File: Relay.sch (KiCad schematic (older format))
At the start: 0 parts

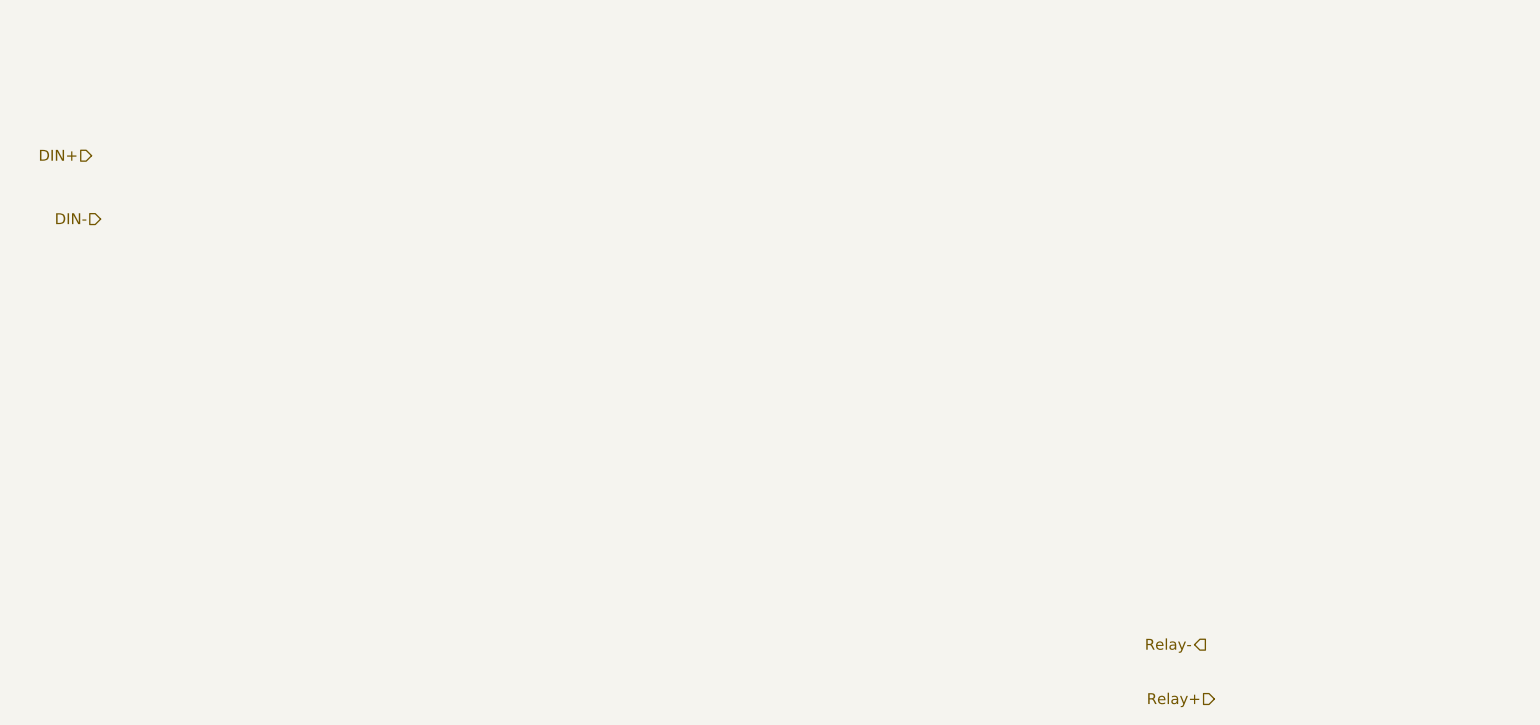
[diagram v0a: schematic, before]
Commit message: Added Powercontrol stuff
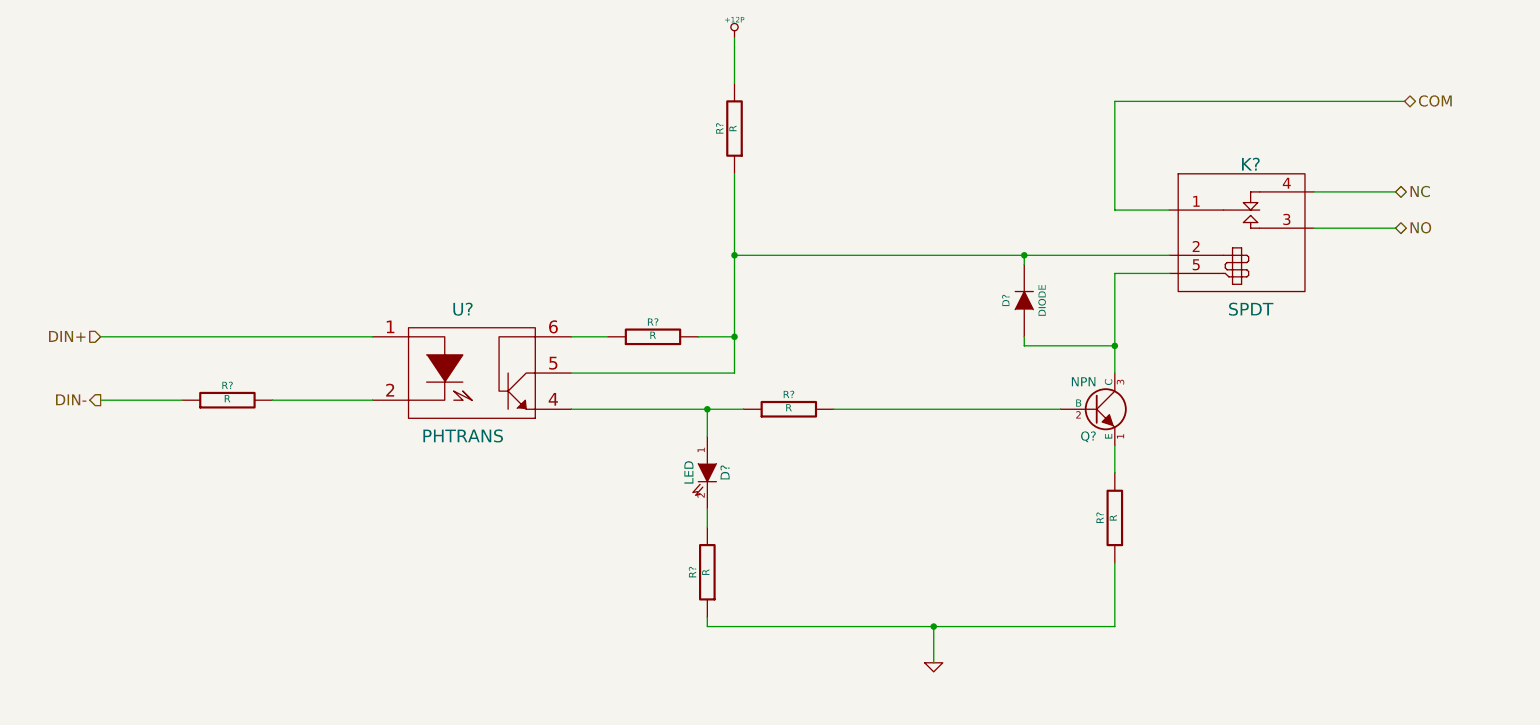
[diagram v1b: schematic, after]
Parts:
- added D?: LED, ~, symbol LED
- added D?: DIODE, ~, symbol DIODE
- added K?: SPDT, ~, symbol SPDT
- added Q?: NPN, ~, symbol NPN
- added R? (x6): R, ~, symbol R
- added U?: PHTRANS, ~, symbol PHTRANS
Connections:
- net DIN+: now also U?.1
- net DIN-: now also R?.1
- new net: R?.2, U?.2
- new net: D?.1 (A), R?.1, U?.4
- new net: D?.2 (K), K?.2 (COIL+), R?.1, R?.2, U?.5
- new net: R?.1, U?.6
- new net: Q?.2 (B), R?.2
- new net: Q?.1 (E), R?.2
- new net: D?.1 (A), K?.5 (COIL-), Q?.3 (C)
- new net: D?.2 (K), R?.2
- new net +12P: R?.2
- new net COM: K?.1 (COM)
- new net GND: R?.1, R?.1
- new net NC: K?.4 (NC)
- new net NO: K?.3 (NO)
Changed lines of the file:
@@
 LIBS:contrib
 LIBS:valves
+LIBS:BenchBuddy
 LIBS:BenchBuddy-cache
 EELAYER 27 0
@@
 $Descr A4 11693 8268
 encoding utf-8
-Sheet 4 8
+Sheet 4 9
 Title ""
-Date "31 jan 2014"
+Date "4 feb 2014"
 Rev ""
 Comp ""
@@
 Comment4 ""
 $EndDescr
-Text HLabel 2800 1950 0    60   Input ~ 0
+Text HLabel 2850 2950 0    60   Input ~ 0
 DIN+
-Text HLabel 2850 2300 0    60   Input ~ 0
+Text HLabel 2850 3300 0    60   Output ~ 0
 DIN-
-Text HLabel 8950 4650 0    60   Output ~ 0
-Relay-
-Text HLabel 9000 4950 0    60   Input ~ 0
-Relay+
+Text HLabel 10000 2350 2    60   BiDi ~ 0
+NO
+Text HLabel 10000 2150 2    60   BiDi ~ 0
+NC
+$Comp
+L PHTRANS U?
+U 1 1 52F0ACE1
+P 4900 3150
+F 0 "U?" H 4850 3500 70  0000 C CNN
+F 1 "PHTRANS" H 4850 2800 70  0000 C CNN
+F 2 "~" H 4900 3150 60  0000 C CNN
+F 3 "~" H 4900 3150 60  0000 C CNN
+	1    4900 3150
+	1    0    0    -1
+$EndComp
+$Comp
+L R R?
+U 1 1 52F0AD0D
+P 6650 3350
+F 0 "R?" V 6730 3350 40  0000 C CNN
+F 1 "R" V 6657 3351 40  0000 C CNN
+F 2 "~" V 6580 3350 30  0000 C CNN
+F 3 "~" H 6650 3350 30  0000 C CNN
+	1    6650 3350
+	0    -1   -1   0
+$EndComp
+$Comp
+L NPN Q?
+U 1 1 52F0AD1C
+P 8350 3350
+F 0 "Q?" H 8350 3200 50  0000 R CNN
+F 1 "NPN" H 8350 3500 50  0000 R CNN
+F 2 "~" H 8350 3350 60  0000 C CNN
+F 3 "~" H 8350 3350 60  0000 C CNN
+	1    8350 3350
+	1    0    0    -1
+$EndComp
+$Comp
+L LED D?
+U 1 1 52F0AD2B
+P 6200 3700
+F 0 "D?" H 6200 3800 50  0000 C CNN
+F 1 "LED" H 6200 3600 50  0000 C CNN
+F 2 "~" H 6200 3700 60  0000 C CNN
+F 3 "~" H 6200 3700 60  0000 C CNN
+	1    6200 3700
+	0    1    1    0
+$EndComp
+$Comp
+L SPDT K?
+U 1 1 52F0B440
+P 9200 2450
+F 0 "K?" H 9200 2900 70  0000 C CNN
+F 1 "SPDT" H 9200 2100 70  0000 C CNN
+F 2 "~" H 9150 2700 60  0000 C CNN
+F 3 "~" H 9150 2700 60  0000 C CNN
+	1    9200 2450
+	1    0    0    -1
+$EndComp
+Text HLabel 10050 1650 2    60   BiDi ~ 0
+COM
+Wire Wire Line
+	10000 2150 9550 2150
+Wire Wire Line
+	10000 2350 9550 2350
+Wire Wire Line
+	5450 3350 6400 3350
+$Comp
+L R R?
+U 1 1 52F0B4B2
+P 8450 3950
+F 0 "R?" V 8530 3950 40  0000 C CNN
+F 1 "R" V 8457 3951 40  0000 C CNN
+F 2 "~" V 8380 3950 30  0000 C CNN
+F 3 "~" H 8450 3950 30  0000 C CNN
+	1    8450 3950
+	-1   0    0    1
+$EndComp
+$Comp
+L GND #PWR?
+U 1 1 52F0B4BA
+P 7450 4750
+F 0 "#PWR?" H 7450 4750 30  0001 C CNN
+F 1 "GND" H 7450 4680 30  0001 C CNN
+F 2 "" H 7450 4750 60  0000 C CNN
+F 3 "" H 7450 4750 60  0000 C CNN
+	1    7450 4750
+	1    0    0    -1
+$EndComp
+Wire Wire Line
+	8450 3550 8450 3700
+$Comp
+L R R?
+U 1 1 52F0B4EC
+P 6350 1800
+F 0 "R?" V 6430 1800 40  0000 C CNN
+F 1 "R" V 6357 1801 40  0000 C CNN
+F 2 "~" V 6280 1800 30  0000 C CNN
+F 3 "~" H 6350 1800 30  0000 C CNN
+	1    6350 1800
+	-1   0    0    1
+$EndComp
+$Comp
+L R R?
+U 1 1 52F0B501
+P 6200 4250
+F 0 "R?" V 6280 4250 40  0000 C CNN
+F 1 "R" V 6207 4251 40  0000 C CNN
+F 2 "~" V 6130 4250 30  0000 C CNN
+F 3 "~" H 6200 4250 30  0000 C CNN
+	1    6200 4250
+	-1   0    0    1
+$EndComp
+Wire Wire Line
+	6200 3350 6200 3500
+Wire Wire Line
+	6200 3900 6200 4000
+Wire Wire Line
+	6200 4500 6200 4550
+Wire Wire Line
+	6200 4550 8450 4550
+Connection ~ 7450 4550
+Wire Wire Line
+	6350 2050 6350 3150
+Connection ~ 6350 2500
+$Comp
+L R R?
+U 1 1 52F0B56E
+P 5900 2950
+F 0 "R?" V 5980 2950 40  0000 C CNN
+F 1 "R" V 5907 2951 40  0000 C CNN
+F 2 "~" V 5830 2950 30  0000 C CNN
+F 3 "~" H 5900 2950 30  0000 C CNN
+	1    5900 2950
+	0    -1   -1   0
+$EndComp
+Wire Wire Line
+	6350 3150 5450 3150
+Connection ~ 6200 3350
+Wire Wire Line
+	6150 2950 6350 2950
+Connection ~ 6350 2950
+Wire Wire Line
+	5650 2950 5450 2950
+Wire Wire Line
+	6350 1300 6350 1550
+$Comp
+L R R?
+U 1 1 52F0B602
+P 3550 3300
+F 0 "R?" V 3630 3300 40  0000 C CNN
+F 1 "R" V 3557 3301 40  0000 C CNN
+F 2 "~" V 3480 3300 30  0000 C CNN
+F 3 "~" H 3550 3300 30  0000 C CNN
+	1    3550 3300
+	0    -1   -1   0
+$EndComp
+Wire Wire Line
+	2850 2950 4350 2950
+Wire Wire Line
+	2850 3300 3300 3300
+Wire Wire Line
+	3800 3300 4350 3300
+Wire Wire Line
+	8750 2500 6350 2500
+Wire Wire Line
+	8450 2600 8450 3150
+Wire Wire Line
+	8750 2250 8450 2250
+Wire Wire Line
+	8450 2250 8450 1650
+Wire Wire Line
+	8450 1650 10050 1650
+Wire Wire Line
+	8150 3350 6900 3350
+Wire Wire Line
+	7450 4550 7450 4750
+Wire Wire Line
+	8450 4550 8450 4200
+Wire Wire Line
+	8750 2600 8450 2600
+$Comp
+L DIODE D?
+U 1 1 52F0B784
+P 7950 2750
+F 0 "D?" H 7950 2850 40  0000 C CNN
+F 1 "DIODE" H 7950 2650 40  0000 C CNN
+F 2 "~" H 7950 2750 60  0000 C CNN
+F 3 "~" H 7950 2750 60  0000 C CNN
+	1    7950 2750
+	0    -1   -1   0
+$EndComp
+Wire Wire Line
+	7950 2550 7950 2500
+Connection ~ 7950 2500
+Wire Wire Line
+	7950 2950 7950 3000
+Wire Wire Line
+	7950 3000 8450 3000
+Connection ~ 8450 3000
+$Comp
+L +12P #PWR?
+U 1 1 52F1085D
+P 6350 1300
+F 0 "#PWR?" H 6350 1270 30  0001 C CNN
+F 1 "+12P" H 6350 1400 30  0000 C CNN
+F 2 "" H 6350 1300 60  0000 C CNN
+F 3 "" H 6350 1300 60  0000 C CNN
+	1    6350 1300
+	1    0    0    -1
+$EndComp
 $EndSCHEMATC

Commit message: Struktur nach Arduino
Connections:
- net COM renamed RELAY_COM
- net DIN+ renamed RELAY+
- net DIN- renamed RELAY-
- net NC renamed RELAY_NC
- net NO renamed RELAY_NO
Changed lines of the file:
@@
 Sheet 4 9
 Title ""
-Date "4 feb 2014"
+Date "6 feb 2014"
 Rev ""
 Comp ""
@@
 $EndDescr
 Text HLabel 2850 2950 0    60   Input ~ 0
-DIN+
+RELAY+
 Text HLabel 2850 3300 0    60   Output ~ 0
-DIN-
+RELAY-
 Text HLabel 10000 2350 2    60   BiDi ~ 0
-NO
+RELAY_NO
 Text HLabel 10000 2150 2    60   BiDi ~ 0
-NC
+RELAY_NC
 $Comp
 L PHTRANS U?
@@
 $EndComp
 Text HLabel 10050 1650 2    60   BiDi ~ 0
-COM
+RELAY_COM
 Wire Wire Line
 	10000 2150 9550 2150

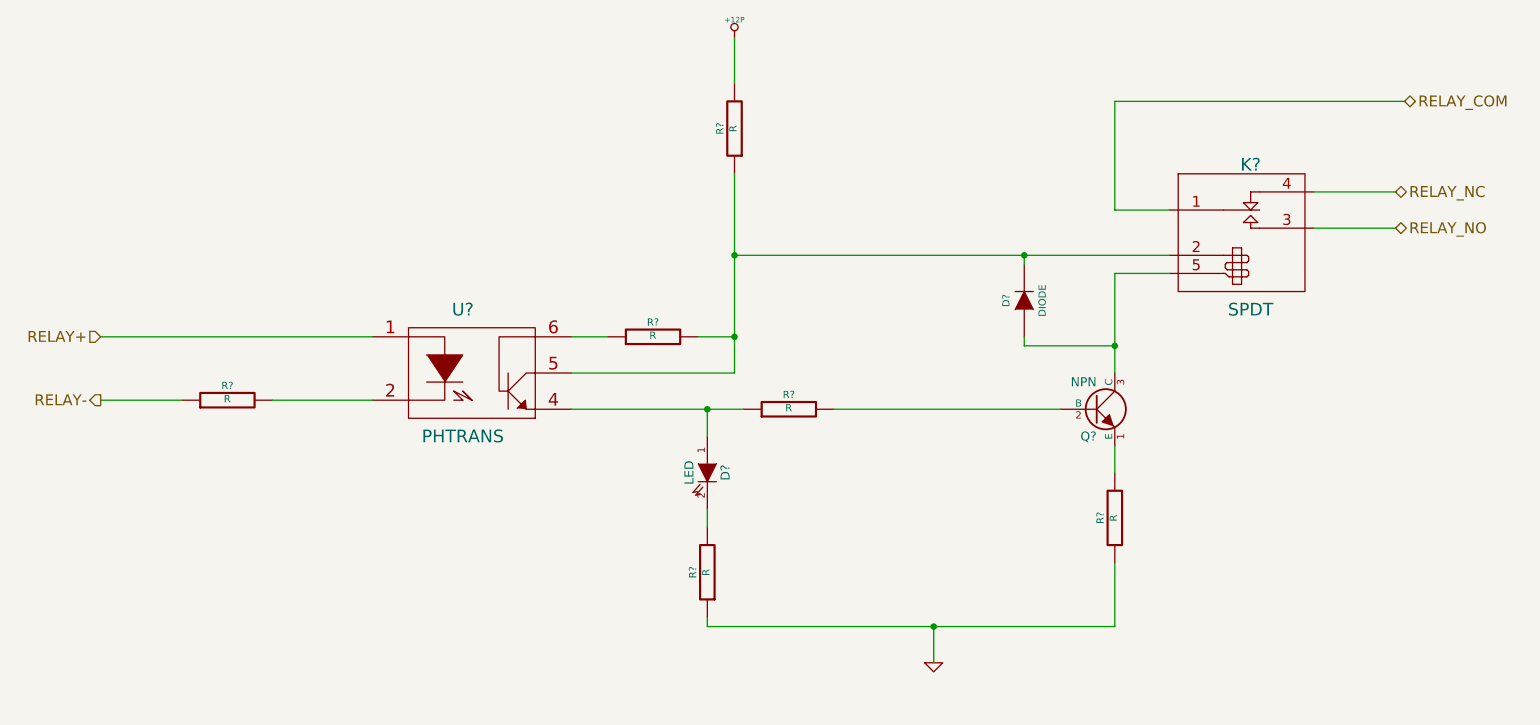
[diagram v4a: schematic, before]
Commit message: Nach Einfuegen Relay-Modul
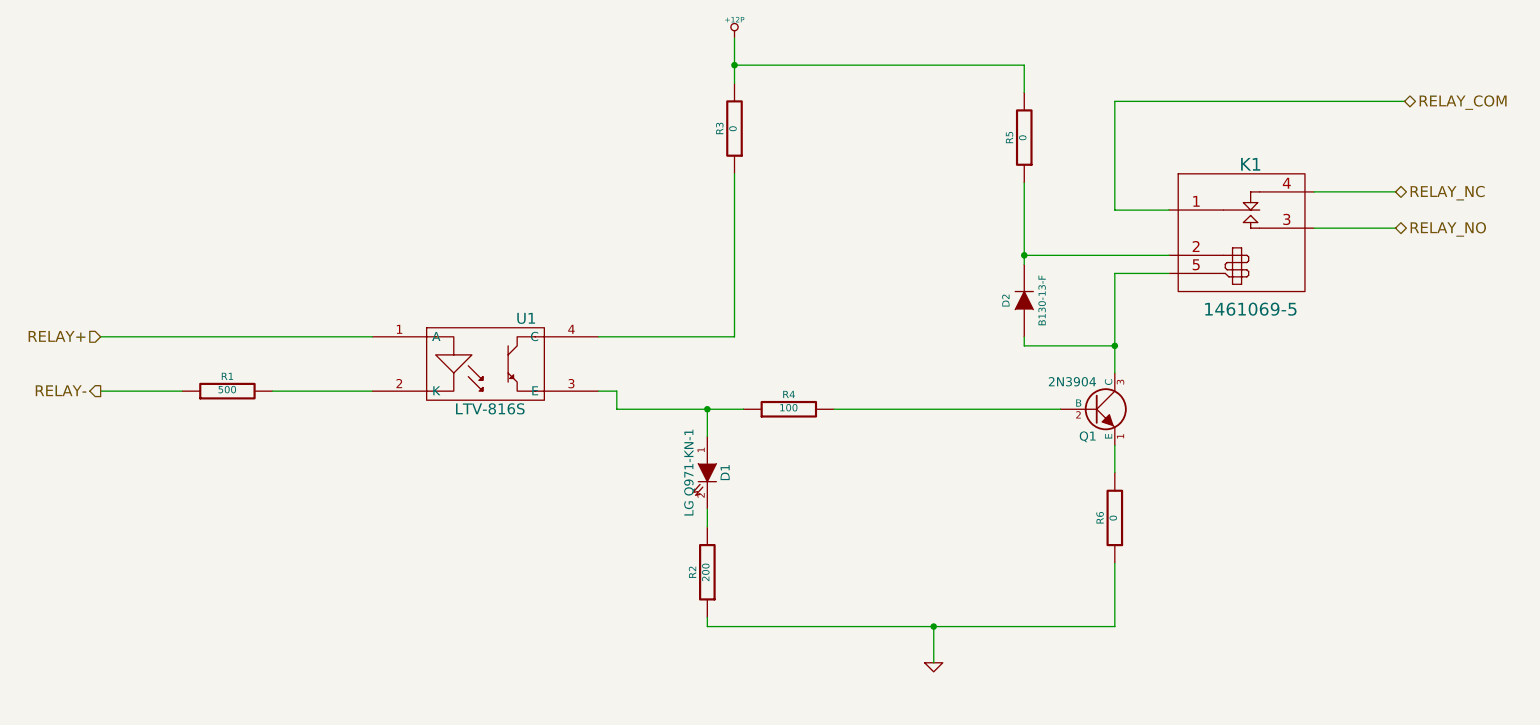
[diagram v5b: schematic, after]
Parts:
- removed R?: R, ~, symbol R
- removed U?: PHTRANS, ~, symbol PHTRANS
- added R5: 0, ~, symbol R
- added U1: LTV-816S, ~, symbol OPTO-TRANSISTOR4
- D1: renamed from D?; value LED -> LG Q971-KN-1
- D2: renamed from D?; value DIODE -> B130-13-F
- K1: renamed from K?; value SPDT -> 1461069-5
- Q1: renamed from Q?; value NPN -> 2N3904; MFG Name (none) -> Diodes Inc; MFG Part Number (none) -> MMBT3904-7-F
- R1: renamed from R?; value R -> 500
- R2: renamed from R?; value R -> 200
- R3, R6: renamed from R?; value R -> 0
- R4: renamed from R?; value R -> 100
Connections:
- net +12P: now also R5.2
- net RELAY+: now also U1.1 (A)
- net at R1.2: now also U1.2 (K)
- net at D1.1 (A), R4.1: now also U1.3 (E)
- net at D2.2 (K), K1.2 (COIL+): now also R5.1; no longer R3.1
- new net: R3.1, U1.4 (C)
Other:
- moved on the sheet: R1
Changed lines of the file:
@@
 $Descr A4 11693 8268
 encoding utf-8
-Sheet 4 9
+Sheet 3 9
 Title ""
-Date "14 feb 2014"
+Date "17 feb 2014"
 Rev ""
 Comp ""
@@
 Text HLabel 2850 2950 0    60   Input ~ 0
 RELAY+
-Text HLabel 2850 3300 0    60   Output ~ 0
+Text HLabel 2850 3250 0    60   Output ~ 0
 RELAY-
 Text HLabel 10000 2350 2    60   BiDi ~ 0
@@
 RELAY_NC
 $Comp
-L PHTRANS U?
-U 1 1 52F0ACE1
-P 4900 3150
-F 0 "U?" H 4850 3500 70  0000 C CNN
-F 1 "PHTRANS" H 4850 2800 70  0000 C CNN
-F 2 "~" H 4900 3150 60  0000 C CNN
-F 3 "~" H 4900 3150 60  0000 C CNN
-	1    4900 3150
-	1    0    0    -1
-$EndComp
-$Comp
-L R R?
+L R R4
 U 1 1 52F0AD0D
 P 6650 3350
-F 0 "R?" V 6730 3350 40  0000 C CNN
-F 1 "R" V 6657 3351 40  0000 C CNN
+F 0 "R4" V 6730 3350 40  0000 C CNN
+F 1 "100" V 6657 3351 40  0000 C CNN
 F 2 "~" V 6580 3350 30  0000 C CNN
 F 3 "~" H 6650 3350 30  0000 C CNN
@@
 $EndComp
 $Comp
-L NPN Q?
+L NPN Q1
 U 1 1 52F0AD1C
 P 8350 3350
-F 0 "Q?" H 8350 3200 50  0000 R CNN
-F 1 "NPN" H 8350 3500 50  0000 R CNN
+F 0 "Q1" H 8350 3200 50  0000 R CNN
+F 1 "2N3904" H 8350 3500 50  0000 R CNN
 F 2 "~" H 8350 3350 60  0000 C CNN
 F 3 "~" H 8350 3350 60  0000 C CNN
+F 4 "Diodes Inc" H 8350 3350 60  0001 C CNN "MFG Name"
+F 5 "MMBT3904-7-F" H 8350 3350 60  0001 C CNN "MFG Part Number"
 	1    8350 3350
 	1    0    0    -1
 $EndComp
 $Comp
-L LED D?
+L LED D1
 U 1 1 52F0AD2B
 P 6200 3700
-F 0 "D?" H 6200 3800 50  0000 C CNN
-F 1 "LED" H 6200 3600 50  0000 C CNN
+F 0 "D1" H 6200 3800 50  0000 C CNN
+F 1 "LG Q971-KN-1" H 6200 3600 50  0000 C CNN
 F 2 "~" H 6200 3700 60  0000 C CNN
 F 3 "~" H 6200 3700 60  0000 C CNN
@@
 $EndComp
 $Comp
-L SPDT K?
+L SPDT K1
 U 1 1 52F0B440
 P 9200 2450
-F 0 "K?" H 9200 2900 70  0000 C CNN
-F 1 "SPDT" H 9200 2100 70  0000 C CNN
+F 0 "K1" H 9200 2900 70  0000 C CNN
+F 1 "1461069-5" H 9200 2100 70  0000 C CNN
 F 2 "~" H 9150 2700 60  0000 C CNN
 F 3 "~" H 9150 2700 60  0000 C CNN
@@
 Wire Wire Line
 	10000 2350 9550 2350
-Wire Wire Line
-	5450 3350 6400 3350
-$Comp
-L R R?
+$Comp
+L R R6
 U 1 1 52F0B4B2
 P 8450 3950
-F 0 "R?" V 8530 3950 40  0000 C CNN
-F 1 "R" V 8457 3951 40  0000 C CNN
+F 0 "R6" V 8530 3950 40  0000 C CNN
+F 1 "0" V 8457 3951 40  0000 C CNN
 F 2 "~" V 8380 3950 30  0000 C CNN
 F 3 "~" H 8450 3950 30  0000 C CNN
@@
 $EndComp
 $Comp
-L GND #PWR?
+L GND #PWR12
 U 1 1 52F0B4BA
 P 7450 4750
-F 0 "#PWR?" H 7450 4750 30  0001 C CNN
+F 0 "#PWR12" H 7450 4750 30  0001 C CNN
 F 1 "GND" H 7450 4680 30  0001 C CNN
 F 2 "" H 7450 4750 60  0000 C CNN
@@
 	8450 3550 8450 3700
 $Comp
-L R R?
+L R R3
 U 1 1 52F0B4EC
 P 6350 1800
-F 0 "R?" V 6430 1800 40  0000 C CNN
-F 1 "R" V 6357 1801 40  0000 C CNN
+F 0 "R3" V 6430 1800 40  0000 C CNN
+F 1 "0" V 6357 1801 40  0000 C CNN
 F 2 "~" V 6280 1800 30  0000 C CNN
 F 3 "~" H 6350 1800 30  0000 C CNN
@@
 $EndComp
 $Comp
-L R R?
+L R R2
 U 1 1 52F0B501
 P 6200 4250
-F 0 "R?" V 6280 4250 40  0000 C CNN
-F 1 "R" V 6207 4251 40  0000 C CNN
+F 0 "R2" V 6280 4250 40  0000 C CNN
+F 1 "200" V 6207 4251 40  0000 C CNN
 F 2 "~" V 6130 4250 30  0000 C CNN
 F 3 "~" H 6200 4250 30  0000 C CNN
@@
 	6200 4550 8450 4550
 Connection ~ 7450 4550
-Wire Wire Line
-	6350 2050 6350 3150
-Connection ~ 6350 2500
-$Comp
-L R R?
-U 1 1 52F0B56E
-P 5900 2950
-F 0 "R?" V 5980 2950 40  0000 C CNN
-F 1 "R" V 5907 2951 40  0000 C CNN
-F 2 "~" V 5830 2950 30  0000 C CNN
-F 3 "~" H 5900 2950 30  0000 C CNN
-	1    5900 2950
+Connection ~ 6200 3350
+Wire Wire Line
+	5600 2950 6350 2950
+Wire Wire Line
+	6350 1300 6350 1550
+$Comp
+L R R1
+U 1 1 52F0B602
+P 3550 3250
+F 0 "R1" V 3630 3250 40  0000 C CNN
+F 1 "500" V 3557 3251 40  0000 C CNN
+F 2 "~" V 3480 3250 30  0000 C CNN
+F 3 "~" H 3550 3250 30  0000 C CNN
+	1    3550 3250
 	0    -1   -1   0
 $EndComp
 Wire Wire Line
-	6350 3150 5450 3150
-Connection ~ 6200 3350
-Wire Wire Line
-	6150 2950 6350 2950
-Connection ~ 6350 2950
-Wire Wire Line
-	5650 2950 5450 2950
-Wire Wire Line
-	6350 1300 6350 1550
-$Comp
-L R R?
-U 1 1 52F0B602
-P 3550 3300
-F 0 "R?" V 3630 3300 40  0000 C CNN
-F 1 "R" V 3557 3301 40  0000 C CNN
-F 2 "~" V 3480 3300 30  0000 C CNN
-F 3 "~" H 3550 3300 30  0000 C CNN
-	1    3550 3300
-	0    -1   -1   0
-$EndComp
-Wire Wire Line
 	2850 2950 4350 2950
 Wire Wire Line
-	2850 3300 3300 3300
-Wire Wire Line
-	3800 3300 4350 3300
-Wire Wire Line
-	8750 2500 6350 2500
+	2850 3250 3300 3250
 Wire Wire Line
 	8450 2600 8450 3150
@@
 	8750 2600 8450 2600
 $Comp
-L DIODE D?
+L DIODE D2
 U 1 1 52F0B784
 P 7950 2750
-F 0 "D?" H 7950 2850 40  0000 C CNN
-F 1 "DIODE" H 7950 2650 40  0000 C CNN
+F 0 "D2" H 7950 2850 40  0000 C CNN
+F 1 "B130-13-F" H 7950 2650 40  0000 C CNN
 F 2 "~" H 7950 2750 60  0000 C CNN
 F 3 "~" H 7950 2750 60  0000 C CNN
@@
 $EndComp
 Wire Wire Line
-	7950 2550 7950 2500
-Connection ~ 7950 2500
-Wire Wire Line
 	7950 2950 7950 3000
 Wire Wire Line
@@
 Connection ~ 8450 3000
 $Comp
-L +12P #PWR?
+L +12P #PWR11
 U 1 1 52F1085D
 P 6350 1300
-F 0 "#PWR?" H 6350 1270 30  0001 C CNN
+F 0 "#PWR11" H 6350 1270 30  0001 C CNN
 F 1 "+12P" H 6350 1400 30  0000 C CNN
 F 2 "" H 6350 1300 60  0000 C CNN
@@
 	1    0    0    -1
 $EndComp
+$Comp
+L OPTO-TRANSISTOR4 U1
+U 1 1 53021D51
+P 5000 3100
+F 0 "U1" H 5200 3350 60  0000 C CNN
+F 1 "LTV-816S" H 5000 2850 60  0000 C CNN
+F 2 "~" H 5000 3100 60  0000 C CNN
+F 3 "~" H 5000 3100 60  0000 C CNN
+F 4 "LTV-816S" H 5000 3100 60  0001 C CNN "MFG Part Number"
+	1    5000 3100
+	1    0    0    -1
+$EndComp
+Wire Wire Line
+	4350 3250 3800 3250
+Wire Wire Line
+	5700 3350 6400 3350
+Wire Wire Line
+	5700 3350 5700 3250
+Wire Wire Line
+	5700 3250 5600 3250
+Wire Wire Line
+	6350 2950 6350 2050
+Wire Wire Line
+	8750 2500 7950 2500
+Wire Wire Line
+	7950 2100 7950 2550
+$Comp
+L R R5
+U 1 1 53021F4D
+P 7950 1850
+F 0 "R5" V 8030 1850 40  0000 C CNN
+F 1 "0" V 7957 1851 40  0000 C CNN
+F 2 "~" V 7880 1850 30  0000 C CNN
+F 3 "~" H 7950 1850 30  0000 C CNN
+	1    7950 1850
+	-1   0    0    1
+$EndComp
+Connection ~ 7950 2500
+Wire Wire Line
+	7950 1600 7950 1450
+Wire Wire Line
+	7950 1450 6350 1450
+Connection ~ 6350 1450
 $EndSCHEMATC
